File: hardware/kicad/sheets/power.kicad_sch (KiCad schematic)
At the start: 27 parts, among them J2 24V_IN, Q8 AO3401A, U11 XL1509-5.0E1, U12 TPS2116DRLR, U2 TLV1117LV33

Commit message: hardware: honest symbols, real MPNs, U6 spares grounded, LCD_RST verified
Third batch from SCHEMATIC-REVIEW-2026-10-22.md (findings 6, 8, 11, 17,
18 and E1/E2).

Symbols: D8 is bisque:SMAJ30A (drawn as a zener with its cathode on the
rail, since the fitted TVS is unidirectional), Q5-Q7 are bisque:CJ2310
and U2 is bisque:TLV1117LV33, each a flattened copy of the stock symbol
with the fitted part's name, description and LCSC-hosted datasheet, so
no pin or wire moved. The stock D_TVS, 2N7002 and TLV1117-33 embeds are
gone from the sheets.

Sourcing: every one of the 160 assembled symbols now carries MPN (the
manufacturer's part number, from LCSC's product record for its C-number),
Manufacturer and Datasheet (LCSC's hosted PDF) beside LCSC. check_mpn.py
keeps LCSC tied to gen_jlc.LCSC and requires the other two to be present
and MPN not to be a bare C-number.

Drawing: J11's IN1_RAW/IN2_RAW labels read along their own wires instead
of across the connector; U6's unused Darlington inputs I4-I7 are tied to
GND (the board's F.Cu pour already covers them - 4 pads re-netted, 0
unconnected, DRC 0); the root notes record the retired designators and
the LCD_RST finding (the MSP4021's own schematic shows no pull-up on
RESET, so GPIO46 does not block download mode); the mcu sheet notes that
GPIO35/36 rule out R8 (octal PSRAM) modules.

The datasheet manifest maps the shared 22uF/25V sheet to the unified
value and exempts the test points' net-name values. Full make pcb-check
passes; gerbers differ by timestamp and the re-filled GND pour; 3D
renders refreshed.

Co-Authored-By: Claude Fable 5.1 <noreply@anthropic.com>
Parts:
- C1, C3, C44, C45: MPN C12891 -> CL31A226KAHNNNE; Manufacturer (none) -> Samsung Electro-Mechanics
- C2, C4, C43: MPN C49678 -> CC0805KRX7R9BB104; Manufacturer (none) -> YAGEO
- C41, C42: MPN C13585 -> CL31A106KBHNNNE; Manufacturer (none) -> Samsung Electro-Mechanics
- C46: MPN C2977550 -> RVT1C101M0505; Manufacturer (none) -> ROQANG
- C47, C48: MPN C52923 -> CL05A105KA5NQNC; Manufacturer (none) -> Samsung Electro-Mechanics
- D11: MPN C22375294 -> BZT52C8V2S; Manufacturer (none) -> R+O
- D7: MPN C8678 -> SS34; Manufacturer (none) -> MDD(Microdiode Semiconductor)
- D8: symbol Device:D_TVS -> bisque:SMAJ30A; MPN C19077547 -> SMAJ30A; Manufacturer (none) -> R+O
- F1: MPN C369169 -> JK-mSMD075-33; Manufacturer (none) -> Jinrui
- J2: MPN C8465 -> WJ500V-5.08-2P; Manufacturer (none) -> KANGNEX
- L1: MPN C475527 -> FXL0650-470-M; Manufacturer (none) -> cjiang
- LED2: MPN C2297 -> KT-0805G; Manufacturer (none) -> Hubei KENTO Elec
- Q8: MPN C15127 -> AO3401A; Manufacturer (none) -> AOS
- R62: MPN C149504 -> 0805W8F1003T5E; Manufacturer (none) -> UNI-ROYAL
- R63: MPN C17621 -> 0805W8F3002T5E; Manufacturer (none) -> UNI-ROYAL
- R64: MPN C17414 -> 0805W8F1002T5E; Manufacturer (none) -> UNI-ROYAL
- R9: MPN C17513 -> 0805W8F1001T5E; Manufacturer (none) -> UNI-ROYAL
- U11: MPN C61063 -> XL1509-5.0E1; Manufacturer (none) -> XLSEMI
- U12: MPN C3235557 -> TPS2116DRLR; Manufacturer (none) -> TI
- U2: symbol Regulator_Linear:TLV1117-33 -> bisque:TLV1117LV33; MPN C48937499 -> TLV1117LV33DCYR; Manufacturer (none) -> JSMSEMI

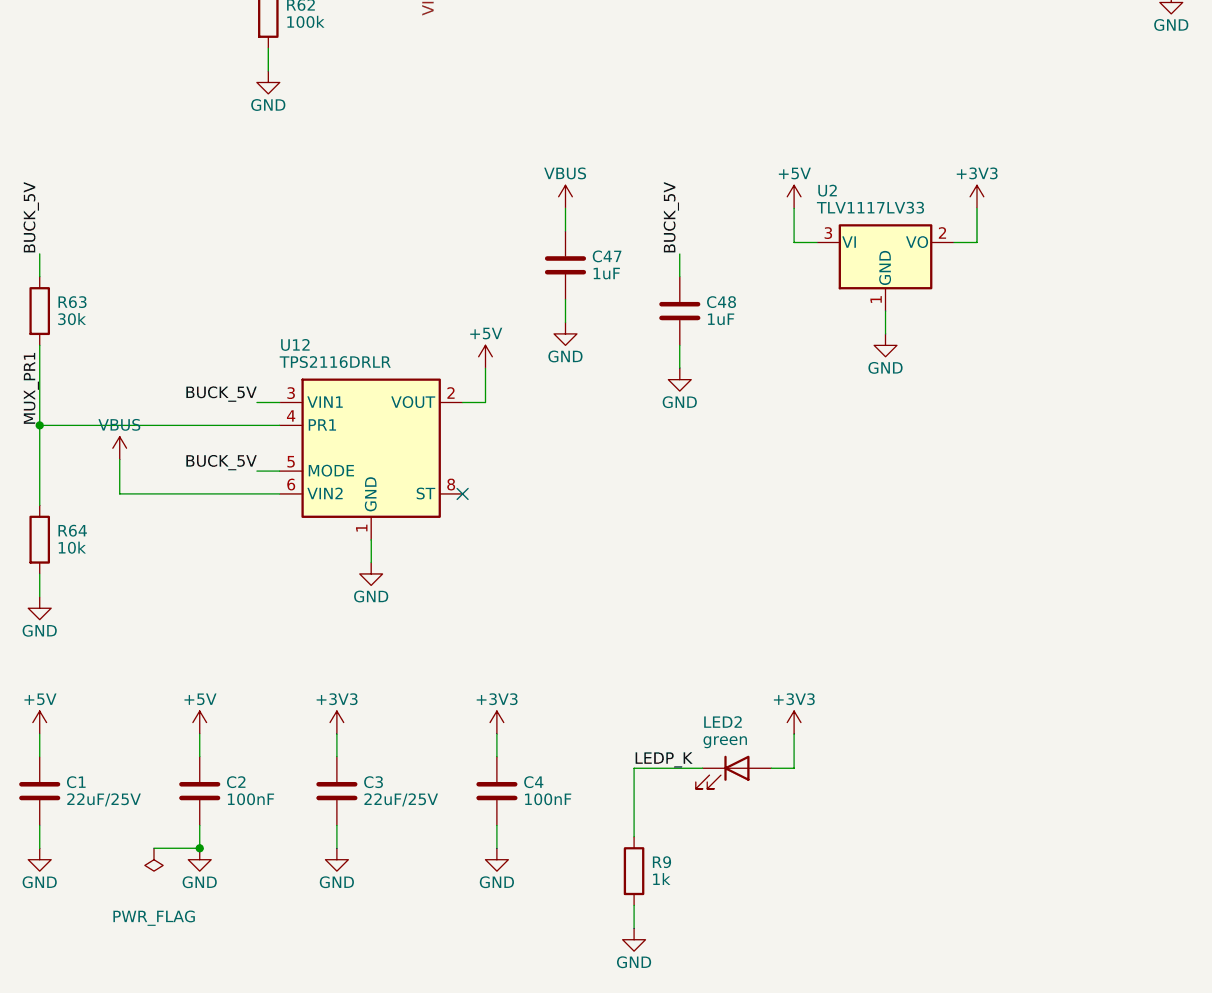
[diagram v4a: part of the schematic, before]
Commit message: hardware: inline front-ends and decoupling at the pins (review 12, 13)
Fourth batch from SCHEMATIC-REVIEW-2026-10-22.md.

Thermocouples: each MAX31856 front-end is an inline chain - the terminal
mirrored so its pins face the IC, K+ and K- on two lines through their
100R, the 100 nF differential cap bridging the lines, the 10 nF caps to
GND off each line, BIAS returned to the raw K- node along the bottom -
and AVDD/DVDD rise to a short +3V3 rail with both 100 nF hanging from
it. The ICs slid 7.62 mm right to make room; nothing else moved.

CT: J12 feeds four lines at 17.78 mm pitch with the 5R1 burden between
each pair, the 1k series parts in the path, the 33 nF to GND off each
filtered node and the 1k references off the N lines; the filtered nodes
end in the CTA_F / CTA_FN / CTB_F labels the ADE7953 pins already
carried. D6 keeps a label-fed clamp block beside the chain. VDD, VINTD
and VINTA each get a rail at the IC's top pin with their two caps on it;
R37/R38 moved 7.62 mm right to clear them.

io: IN1-IN3 are three identical rows - J11 mirrored, 1k in the path, the
10k pull-up above and 100 nF below the node, the hierarchical label at
the end - with D5's clamp block below them.

mcu: C6/C7 hang from U1's 3V3 pin. power: U2 is drawn as an inline
5 V -> 3.3 V chain with C1/C2 on its input and C3/C4 on its output in
the row the caps already occupied; LED2/R9 slid right.

Every pin landed on wiring by construction (the geometry helper checks
each symbol's pins against the wires), ERC is clean, the layout checker
reports no overlaps, the netlist still has 108 nets and the board sync
re-netted nothing. Fab outputs regenerated (schematic PDF, timestamps).

Co-Authored-By: Claude Fable 5.1 <noreply@anthropic.com>
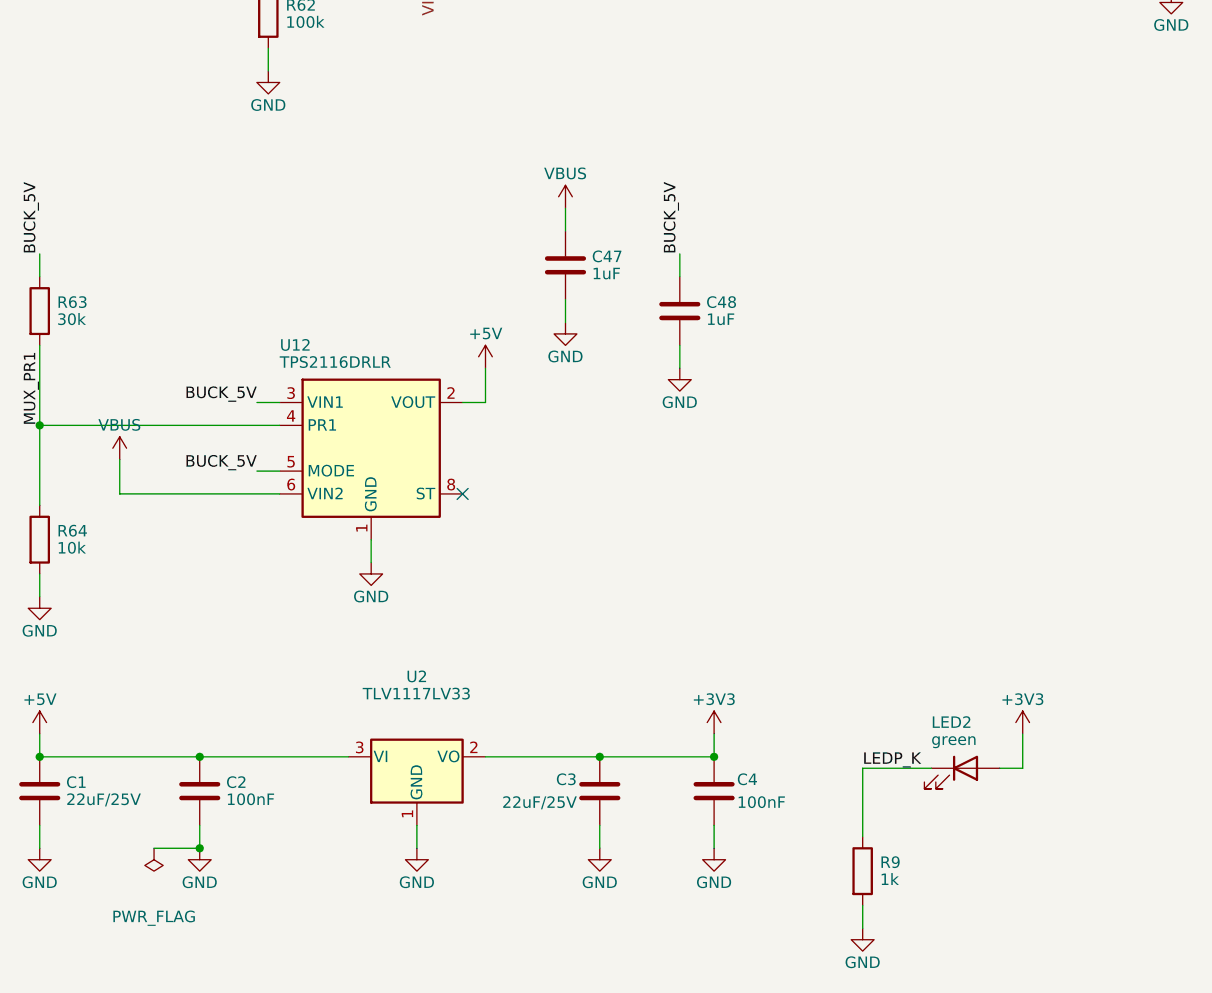
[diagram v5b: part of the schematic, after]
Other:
- moved on the sheet: C3, C4, LED2, R9, U2

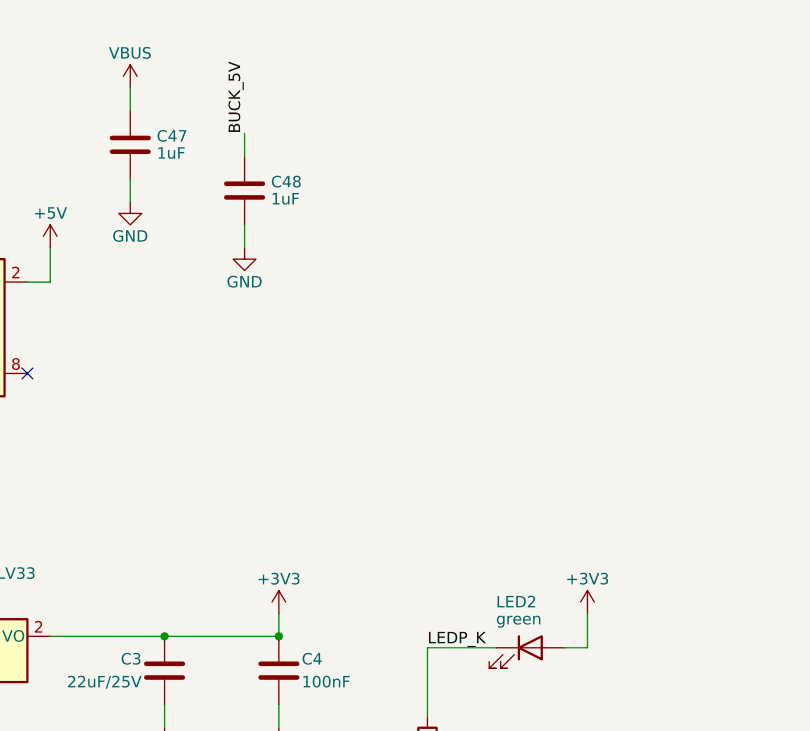
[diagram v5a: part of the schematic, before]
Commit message: hardware: the five quick fixes from the 2026-10-05/10-22 reviews
Schematic (rev B.3, sheets ct/power/mcu/ssr + root):
- R65, 1k from CTA_P to GND, mirrors R33 so the floating CT secondary
  sits at +-V/2 on IAP/IAN and channel A's pin limit is 139 A nominal,
  the same as channel B (schematic review 10-05 item 2).
- D9/D10 freewheel diodes are B5819W (JSCJ C8598, Basic, 1 A / 40 V,
  9 A surge) in the same SOD-123 land, replacing the 1N4148W whose
  150 mA rating never covered a 200 mA contactor coil (PCB review 10-05
  item 12). The SS34 was tried first and does not fit the SSR column.
- ADE_RESET is a hierarchical net to U1 IO37, the spare GPIO; the R30/C37
  RC stays for the power-on stretch (10-22 review E3).
- PWR_STATUS: BUCK_5V through R66 (100k) over R67+R68 (130k) to U1 IO45,
  2.8 V when the 24 V buck runs and 0 V on USB only (10-22 review E4).
  The TPS2116 ST pin would have said the same thing but its pad is boxed
  in by the USB pair on this layout, so it stays unconnected (C3, rev C).

Board:
- Every +5V layer transition (7) now has a second 0.6/0.3 via 0.85 mm
  away with a stub on each layer; the two in the USB corner use 0.3 mm
  stubs (fab-readiness C, "attempted, not landed" -> fixed).
- R65 placed below the CT filters; the divider in the two free columns
  south of U1, lifted 0.75 mm so the nameplate pocket keeps its 16.2 mm
  (it prints at 62% now). BUCK_5V tap hand-routed, the rest by the
  in-house router. DRC 0, make pcb-check ALL CHECKS PASS, 3D re-rendered.

Firmware/docs: KILN_PIN_ADE_RESET (37) and KILN_PIN_PWR_STATUS (45) in
Kconfig with the GPIO45 strapping caveat, check_pinmap NET_KCONFIG,
docs/pin-assignments.md (all 30 GPIOs assigned), DESIGN-NOTES sections
for each change, status notes in the four review documents, gen_jlc
sourcing + JLC_PLACEMENT rows, lcsc_pads cache and datasheet manifest.

Co-Authored-By: Claude Fable 5.1 <noreply@anthropic.com>
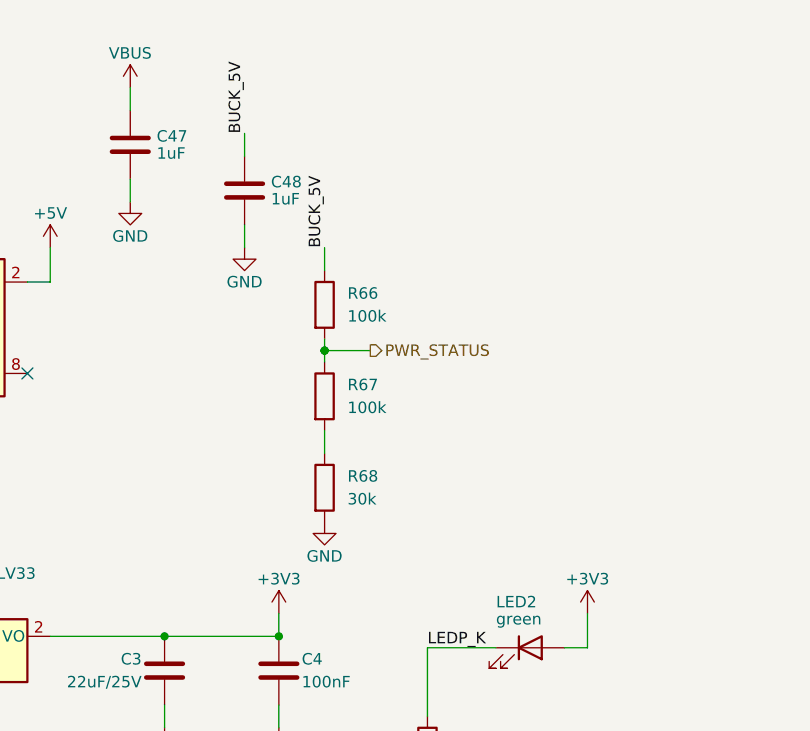
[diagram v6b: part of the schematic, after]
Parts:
- added R66, R67: 100k, Resistor_SMD:R_0805_2012Metric, symbol Device:R
- added R68: 30k, Resistor_SMD:R_0805_2012Metric, symbol Device:R
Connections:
- net BUCK_5V: now also R66.1
- net GND: now also R68.2
- new net: R67.2, R68.1
- new net PWR_STATUS: R66.2, R67.1

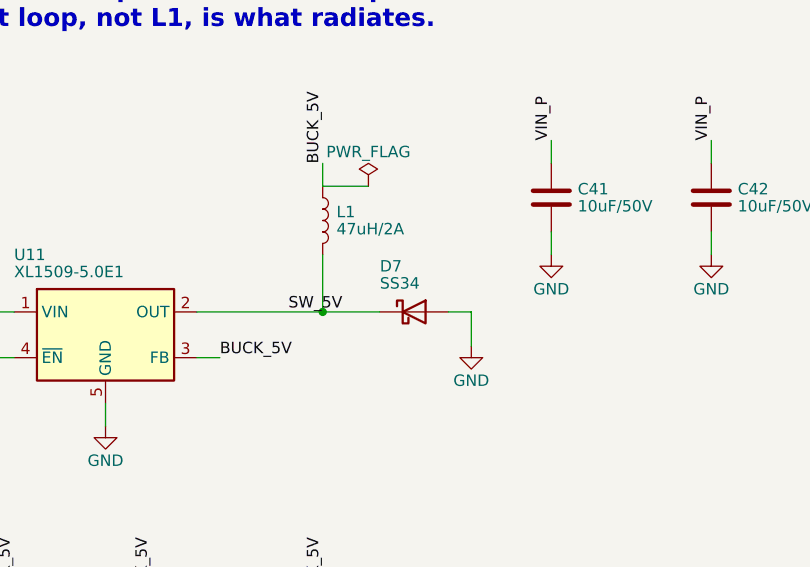
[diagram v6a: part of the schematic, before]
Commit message: hardware: coordinate the input clamp with what sits behind it (review item 1 / PCB item 9)
The reviews flagged D8's 48.4 V clamp against the XL1509's 45 V, the
SS34's 40 V and the AO3401A's 30 V, and asked for an envelope rather
than "it is a surge figure". The envelope is now written at F1 in
DESIGN-NOTES: the supply is the in-enclosure HDR-15-24 or its class
(<= 1 A limit) on wiring that stays in the box, and the SMAJ30A's own
table then bounds the rail at 36.8 V + 1.4 ohm x I - 38.1 V at the
supply's 0.91 A limit, 40 V up to F1's 2.3 A, U11's 45 V abs max only
at 5.8 A, 48.4 V only on the 10/1000 us pulse. The sustained,
current-limited case ends with D8 failing short at <= 38 V, which is
the intended outcome.

The TVS stays. The Mean Well sheet gives the HDR-15-24's trim range as
21.6-29 V, not the +-10% (26.4 V) the notes assumed, so an SMAJ28A would
stand off less than the supply can be set to. Q8 is not stressed in a
forward fault (body diode conducts, D11 clamps the gate). The two parts
with no margin at 38 V were the 40 V diodes that see the rail in
reverse, and both change in the same land:

- D7  SS34  -> SS36 (R+O C7420367), 60 V 3 A SMA. VF 0.70 V vs 0.55 V,
  ~1% of buck efficiency at full load.
- D9/D10 B5819W -> 1N4007W (FUXINSEMI C3018540, SOD-123 body), 1 kV
  1 A. With its channel on the freewheel diode stands off the whole
  rail; a standard-recovery rectifier is the right part for a contactor
  coil at the SSR timer's rate. Drawn with Device:D, not the Schottky
  symbol.

Both are Extended where the old parts were Basic; on Standard PCBA,
where this BOM is, the bill is unchanged (49 lines). lcsc_pads.json
carries both land patterns (resid 0.150 / 0.023 mm), the datasheets
are cached and mapped, SS34/B5819W PDFs recorded as retired. The 26.4 V
trim figure is corrected to 29 V in DESIGN-NOTES, the enclosure README
and the bench smoke test; dated status on both review findings and the
10-22 status table. Still named open: the external SSR input at 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
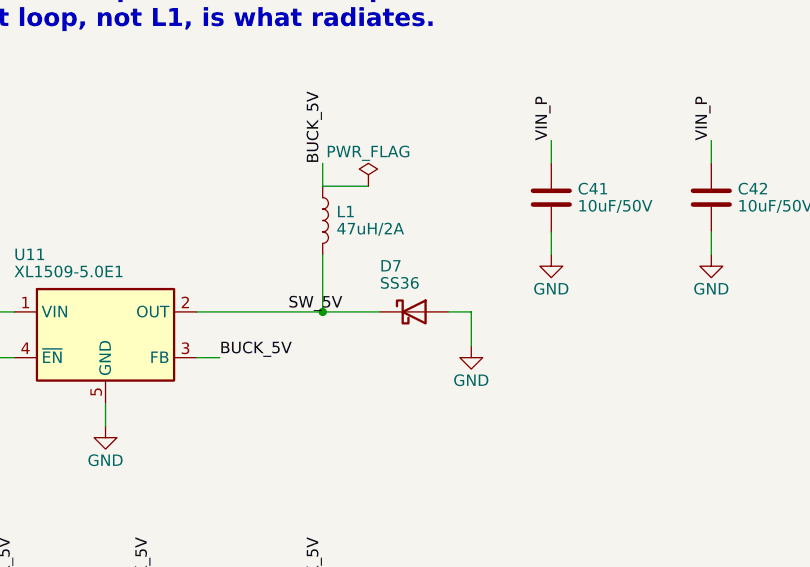
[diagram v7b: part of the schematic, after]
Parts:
- D7: value SS34 -> SS36; LCSC C8678 -> C7420367; MPN SS34 -> SS36; Manufacturer MDD(Microdiode Semiconductor) -> R+O
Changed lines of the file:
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@@
 			)
 		)
-		(property "Value" "SS34"
+		(property "Value" "SS36"
 			(at 204.47 76.83 0)
 			(show_name no)
@@
 			)
 		)
-		(property "Datasheet" "https://datasheet.lcsc.com/datasheet/pdf/dfa1ff67dea875d0135103ba9ada713a.pdf?productCode=C8678"
+		(property "Datasheet" "https://datasheet.lcsc.com/datasheet/pdf/9e763de50d66dc26804ef4c3650380df.pdf?productCode=C7420367"
 			(at 208.28 80.01 0)
 			(hide yes)
@@
 			)
 		)
-		(property "MPN" "SS34"
+		(property "MPN" "SS36"
 			(at 208.28 80.01 0)
 			(hide yes)
@@
 			)
 		)
-		(property "LCSC" "C8678"
+		(property "LCSC" "C7420367"
 			(at 208.28 80.01 0)
 			(hide yes)
@@
 			)
 		)
-		(property "Manufacturer" "MDD(Microdiode Semiconductor)"
+		(property "Manufacturer" "R+O"
 			(at 208.28 80.01 0)
 			(hide yes)
